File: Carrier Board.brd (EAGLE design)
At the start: 90 x 36.1 mm, 54 parts, among them J4 S2B-PH-SM4-TB(LF)(SN), J5 S2B-PH-SM4-TB(LF)(SN), Q1 MMBT2222A, SW2 MF-SW-TACT-6MM, U1 TMP36GRTZ, U2 TPL5010, U3 MB85RC256, U7 NAND

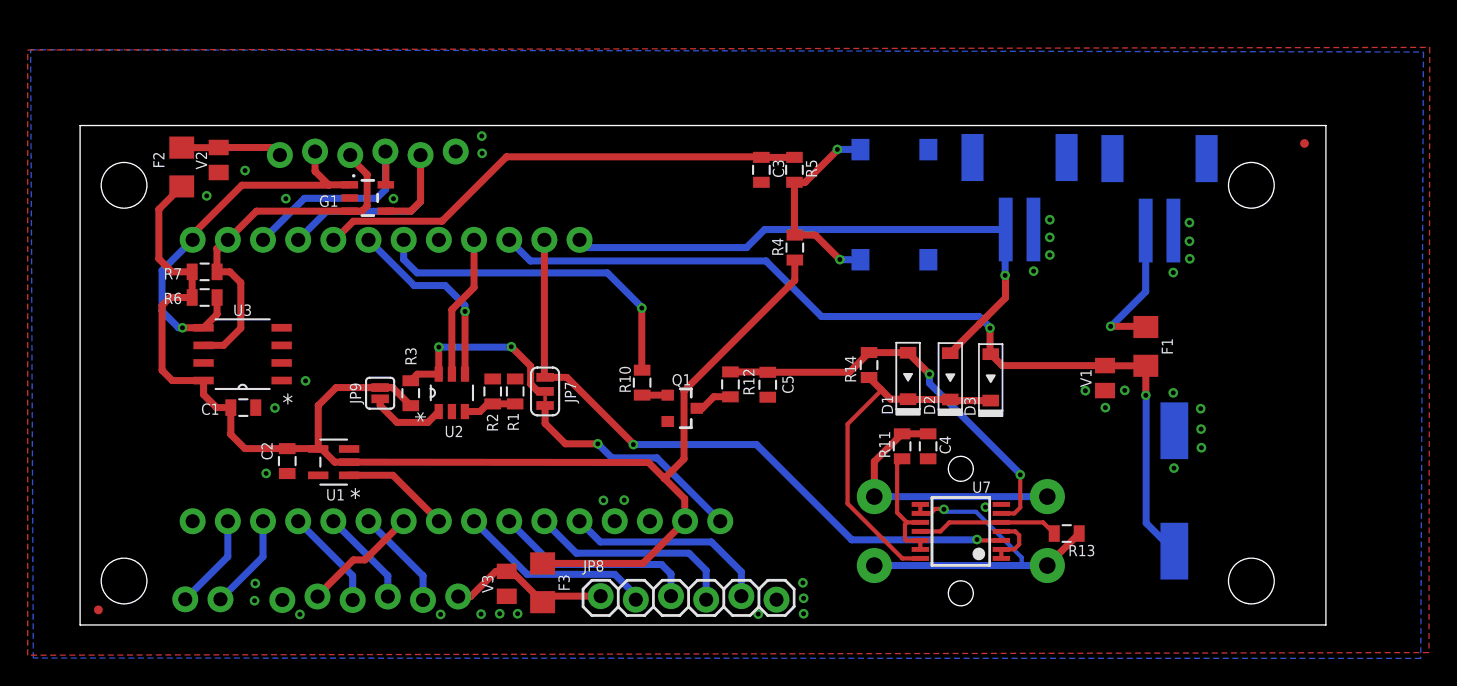
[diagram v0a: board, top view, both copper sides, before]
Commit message: Added 2-Grove Connectors
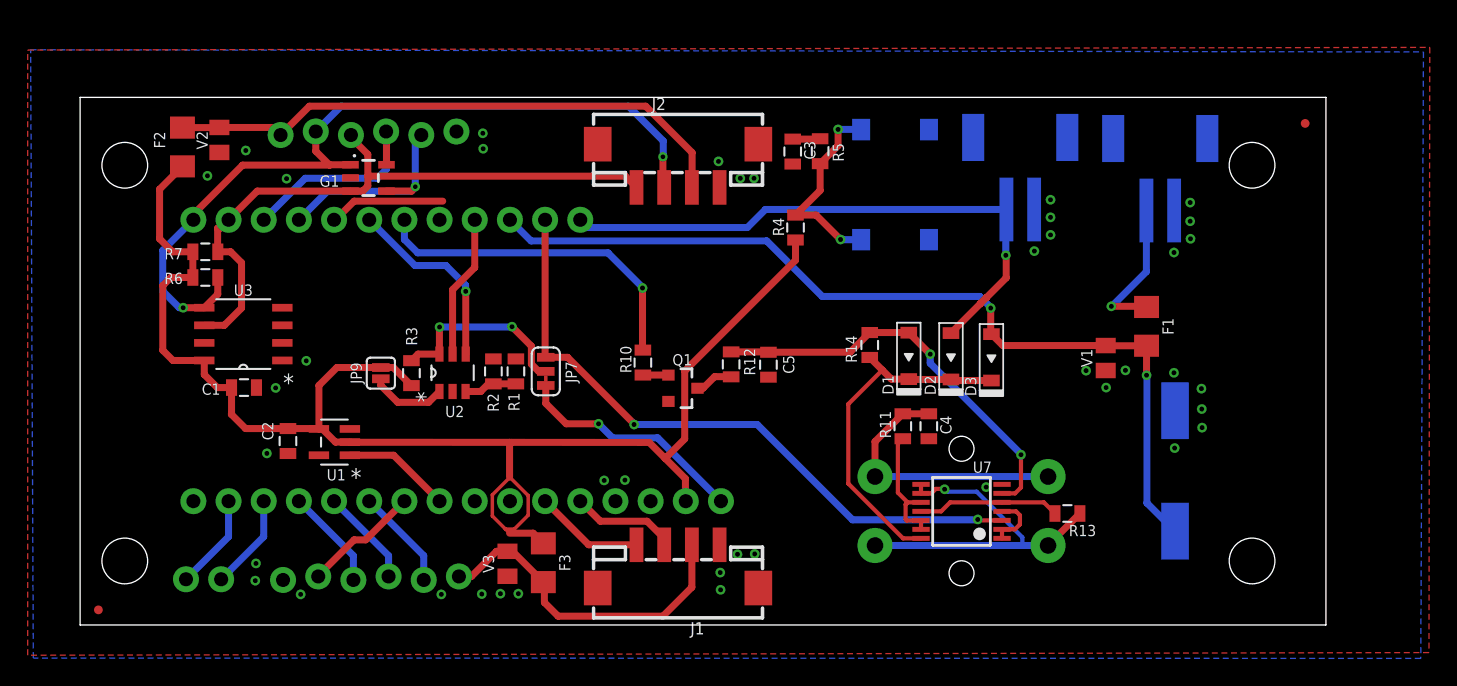
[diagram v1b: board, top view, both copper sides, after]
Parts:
- removed JP8: (no value), SparkFun-Connectors:1X06_LOCK
- added J1, J2: H4P-SMD-2.0, OPL_Connector:HW4-SMD-2.0
- U3: value MB85RC256 -> MB85RC64
- moved C3 2.62 mm to (51.5, 34.2)
- moved R5 2.29 mm to (53.4, 34.2)
- moved C5 1.45 mm to (49.7, 18.8)
- moved D2 1.45 mm to (62.9, 19.4)
- moved D3 1.45 mm to (65.8, 19.3)
- moved JP1 1.45 mm to (27.2, 35.6)
- moved JP3 1.45 mm to (84.6, 33.2)
- moved JP7 1.45 mm to (33.6, 18.3)
- moved Q1 1.45 mm to (43.5, 17.1)
- moved R1 1.45 mm to (31.5, 18.3)
- moved R10 1.45 mm to (40.6, 18.9)
- moved R11 1.45 mm to (59.4, 14.4)
- moved R12 1.45 mm to (47.0, 18.8)
- moved R4 1.45 mm to (51.7, 28.7)
- moved C2 1.45 mm to (15.0, 13.3)
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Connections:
- net A0: now also J1.3; no longer JP8.5
- net A1: now also J1.4; no longer JP8.4
- net A2: no longer JP8.3
- net A3: no longer JP8.2
- net GND: now also J1.1, J1.SS1, J1.SS2, J2.4, J2.SS1, J2.SS2; no longer JP8.6
- net SCL: now also J2.1
- net SDA: now also J2.2
- net VCC-EXT: now also J1.2; no longer JP8.1
- net VCC2-EXT: now also J2.3
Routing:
- net VCC2-EXT: track 7.32 -> 41.8 mm
- net SDA: track 28.2 -> 58.5 mm, vias 1 -> 2
- net USER-SW: track 35.8 -> 10.4 mm
- net SCL: track 26.5 -> 46.3 mm
- net A2: track 14.9 -> 0.00 mm
- net A3: track 14.2 -> 0.00 mm
- net VCC-EXT: track 12.1 -> 24.9 mm
- net A1: track 15.3 -> 7.91 mm
- net A0: track 15.0 -> 7.64 mm
- net D3: track 19.5 -> 15.1 mm, vias 0 -> 1
- net VCC: track 104.7 -> 108.7 mm
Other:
- board size 90 x 36.1 mm -> 90 x 38.1 mm
- board text added: "GND Vcc A0 A1"
- board text removed: "GND A0 A1 A2 A3 Vcc"

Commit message: v1.0 - sent to OSHPark today.
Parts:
- removed BORON: PARTICLE-DEVICES-BORON, Carrier Board:PARTICLE-DEVICES_BORON
- added BORON/ARGON/XENON: PARTICLE-DEVICES-BORON, Carrier Board:PARTICLE-DEVICES_BORON
- moved J4 2.19 mm to (75.9, 34.1)
- moved V1 2.15 mm to (73.7, 21.4), turned to 270 degrees
- moved R13 1.86 mm to (69.5, 8.59)
- moved R5 1.70 mm to (51.8, 34.5)
- moved J5 1.65 mm to (66.3, 34.2)
- moved C8 1.52 mm to (77.6, 11.5)
- moved C3 1.50 mm to (50.0, 34.5)
- moved SW2 1.28 mm to (57.6, 32.2)
- moved J1 0.99 mm to (43.0, 6.76), flipped to the bottom
- moved F2 0.72 mm to (8.05, 34.8)
- moved V2 0.46 mm to (10.4, 35.3)
- moved JP4 0.41 mm to (84.6, 5.03)
- moved JP6 0.41 mm to (3.17, 5.03)
- moved JP3 0.41 mm to (84.6, 33.6)
- moved JP5 0.41 mm to (3.17, 33.6)
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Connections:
- net !RST: now also BORON/ARGON/XENON.RST; no longer BORON.RST
- net A0: now also BORON/ARGON/XENON.A0; no longer BORON.A0
- net A1: now also BORON/ARGON/XENON.A1; no longer BORON.A1
- net A2: now also BORON/ARGON/XENON.A2; no longer BORON.A2
- net A3: now also BORON/ARGON/XENON.A3; no longer BORON.A3
- net D2: now also BORON/ARGON/XENON.D2; no longer BORON.D2
- net D3: now also BORON/ARGON/XENON.D3; no longer BORON.D3
- net DONE: now also BORON/ARGON/XENON.D5; no longer BORON.D5
- net EN: now also BORON/ARGON/XENON.EN; no longer BORON.EN
- net GND: now also BORON/ARGON/XENON.GND; no longer BORON.GND
- net HARD-RESET: now also BORON/ARGON/XENON.D6; no longer BORON.D6
- net LI+: now also BORON/ARGON/XENON.LI+; no longer BORON.LI+
- net MD: now also BORON/ARGON/XENON.MD; no longer BORON.MD
- net MISO: now also BORON/ARGON/XENON.MI; no longer BORON.MI
- net MOSI: now also BORON/ARGON/XENON.MO; no longer BORON.MO
- net RX: now also BORON/ARGON/XENON.RX; no longer BORON.RX
- net SCK: now also BORON/ARGON/XENON.SCK; no longer BORON.SCK
- net SCL: now also BORON/ARGON/XENON.SCL; no longer BORON.SCL
- net SDA: now also BORON/ARGON/XENON.SDA; no longer BORON.SDA
- net SS: now also BORON/ARGON/XENON.A5; no longer BORON.A5
- net TEMP: now also BORON/ARGON/XENON.A4; no longer BORON.A4
- net TX: now also BORON/ARGON/XENON.TX; no longer BORON.TX
- net USER-SW: now also BORON/ARGON/XENON.D4; no longer BORON.D4
- net VCC: now also BORON/ARGON/XENON.3V3; no longer BORON.3V3
- net VUSB: now also BORON/ARGON/XENON.VUSB; no longer BORON.VUSB
- net WAKE: now also BORON/ARGON/XENON.D8; no longer BORON.D8
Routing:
- net USER-SW: track 10.4 -> 36.3 mm
- net VCC: track 108.7 -> 131.9 mm
- net A1: track 7.91 -> 18.1 mm, vias 0 -> 1
- net SCL: track 46.3 -> 54.7 mm, vias 0 -> 1
- net A0: track 7.64 -> 12.8 mm, vias 0 -> 1
- net LI+: track 42.2 -> 38.8 mm
- net DC-IN-EXT: track 10.6 -> 7.98 mm
- net VCC2-EXT: track 41.8 -> 39.7 mm, vias 0 -> 1
- net BUTTON-STATE: track 10.3 -> 8.62 mm
- net VCC-EXT: track 24.9 -> 23.3 mm, vias 0 -> 1
- net N$4: track 14.6 -> 13.3 mm
- net SDA: track 58.5 -> 59.5 mm, vias 2 -> 1
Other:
- board size 90 x 38.1 mm -> 90 x 38.6 mm
- board text added: "A1 A0 Vcc GND"
- board text added: "Power - Push On / Push Off"
- board text added: "SCL SDA VCC GND"
- board text added: "v1.0- 4-15-19"
- board text removed: "GND Vcc A0 A1"
- board text removed: "v1.0- 3-29-19"
